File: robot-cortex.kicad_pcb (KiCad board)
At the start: 4 copper layers, 27.5 x 35.8 mm, 91 parts, among them IC1 THVD2410VDRCR, IC2 THVD2410VDRCR, IC3 THVD2410VDRCR, J1 USB4110GFA, M1 THRU_HOLE_PAD, M2 THRU_HOLE_PAD, Q1 SSM3K15F,LF, Q2 SS8050-G, U1 C2901617, U10 TPS63070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

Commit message: silk
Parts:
- moved R20 0.23 mm to (213.7, 121.3)
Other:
- board text added: "Vbat A B GND"
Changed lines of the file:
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@@
   )
   (footprint "robot-cortex:R_0402_1005Metric" (layer "F.Cu")
-    (at 213.7 121.5565)
+    (at 213.7 121.325)
     (descr "Resistor SMD 0402 (1005 Metric), square (rectangular) end terminal, IPC_7351 nominal, (Body size source: IPC-SM-782 page 72, https://www.pcb-3d.com/wordpress/wp-content/uploads/ipc-sm-782a_amendment_1_and_2.pdf), generated with kicad-footprint-generator")
     (tags "resistor")
@@
     )
   )
+  (gr_line (start 209.375 122.66875) (end 209.375 123.58125)
+    (stroke (width 0.15) (type default)) (layer "F.SilkS"))
+  (gr_line (start 197.75 122.66875) (end 197.75 123.58125)
+    (stroke (width 0.15) (type default)) (layer "F.SilkS"))
+  (gr_line (start 208.425 122.66875) (end 208.425 123.58125)
+    (stroke (width 0.15) (type default)) (layer "F.SilkS"))
+  (gr_line (start 200.6 122.66875) (end 200.6 123.58125)
+    (stroke (width 0.15) (type default)) (layer "F.SilkS"))
+  (gr_line (start 207.45 122.66875) (end 207.45 123.58125)
+    (stroke (width 0.15) (type default)) (layer "F.SilkS"))
+  (gr_line (start 210.3 122.66875) (end 210.3 123.58125)
+    (stroke (width 0.15) (type default)) (layer "F.SilkS"))
+  (gr_line (start 199.675 122.66875) (end 199.675 123.58125)
+    (stroke (width 0.15) (type default)) (layer "F.SilkS"))
+  (gr_line (start 198.725 122.66875) (end 198.725 123.58125)
+    (stroke (width 0.15) (type default)) (layer "F.SilkS"))
   (gr_line (start 191.91 89.7) (end 190.02 91.59)
     (stroke (width 0.1) (type default)) (layer "Edge.Cuts"))
@@
     (effects (font (size 0.762 0.762) (thickness 0.127)) (justify left bottom mirror))
   )
-  (gr_text "3V3" (at 195.75 101.69) (layer "B.SilkS")
+  (gr_text "3V3" (at 195.75 101.015) (layer "B.SilkS")
     (effects (font (size 0.635 0.635) (thickness 0.127)) (justify left bottom mirror))
   )
@@
     (effects (font (size 0.635 0.635) (thickness 0.127)) (justify left bottom mirror))
   )
-  (gr_text "IO0" (at 195.75 99.55) (layer "B.SilkS")
+  (gr_text "IO0" (at 195.75 98.875) (layer "B.SilkS")
     (effects (font (size 0.635 0.635) (thickness 0.127)) (justify left bottom mirror))
   )
@@
     (effects (font (size 0.635 0.635) (thickness 0.127)) (justify left bottom mirror))
   )
-  (gr_text "TDI" (at 195.75 96.6) (layer "B.SilkS")
+  (gr_text "TDI" (at 195.75 95.925) (layer "B.SilkS")
     (effects (font (size 0.635 0.635) (thickness 0.127)) (justify left bottom mirror))
   )
-  (gr_text "GND" (at 195.75 94.55) (layer "B.SilkS")
+  (gr_text "GND" (at 195.75 93.875) (layer "B.SilkS")
     (effects (font (size 0.635 0.635) (thickness 0.127)) (justify left bottom mirror))
   )
@@
     (effects (font (size 0.635 0.635) (thickness 0.127) bold) (justify left bottom mirror))
   )
-  (gr_text "TDO" (at 195.75 98.54) (layer "B.SilkS")
+  (gr_text "TDO" (at 195.75 97.865) (layer "B.SilkS")
     (effects (font (size 0.635 0.635) (thickness 0.127)) (justify left bottom mirror))
   )
@@
     (effects (font (size 0.635 0.635) (thickness 0.127)) (justify left bottom mirror))
   )
-  (gr_text "TMS" (at 195.75 97.57) (layer "B.SilkS")
+  (gr_text "TMS" (at 195.75 96.895) (layer "B.SilkS")
     (effects (font (size 0.635 0.635) (thickness 0.127)) (justify left bottom mirror))
   )
-  (gr_text "TCK" (at 195.75 95.65) (layer "B.SilkS")
+  (gr_text "TCK" (at 195.75 94.975) (layer "B.SilkS")
     (effects (font (size 0.635 0.635) (thickness 0.127)) (justify left bottom mirror))
   )
@@
     (effects (font (size 0.762 0.762) (thickness 0.127)) (justify left bottom mirror))
   )
-  (gr_text "EN" (at 195.75 100.57) (layer "B.SilkS")
+  (gr_text "EN" (at 195.75 99.895) (layer "B.SilkS")
     (effects (font (size 0.635 0.635) (thickness 0.127)) (justify left bottom mirror))
   )
+  (gr_text "Vbat\nA\nB\nGND" (at 200.925 122.50625 90) (layer "F.SilkS")
+    (effects (font (size 0.5842 0.5842) (thickness 0.0762)) (justify left bottom))
+  )
+  (gr_text "Vbat\nA\nB\nGND" (at 210.65 122.50625 90) (layer "F.SilkS")
+    (effects (font (size 0.5842 0.5842) (thickness 0.0762)) (justify left bottom))
+  )
   (gr_text "V3 R1" (at 210.43 91.72) (layer "F.SilkS")
     (effects (font (size 1 1) (thickness 0.2) bold) (justify left bottom))
@@
   (segment (start 203.727432 111.09) (end 204.405 111.09) (width 0.254) (layer "B.Cu") (net 61))
   (segment (start 194.4 116.75) (end 199.825 116.75) (width 0.254) (layer "B.Cu") (net 61))
-  (segment (start 213.45 120.3) (end 213.45 121.4315) (width 0.25) (layer "F.Cu") (net 62))
+  (segment (start 213.325 121.325) (end 213.325 122.4315) (width 0.25) (layer "F.Cu") (net 62))
+  (segment (start 213.45 121.2) (end 213.325 121.325) (width 0.25) (layer "F.Cu") (net 62))
   (segment (start 213.325 122.4315) (end 213.3 122.4565) (width 0.25) (layer "F.Cu") (net 62))
-  (segment (start 213.45 121.4315) (end 213.325 121.5565) (width 0.25) (layer "F.Cu") (net 62))
-  (segment (start 213.325 121.5565) (end 213.325 122.4315) (width 0.25) (layer "F.Cu") (net 62))
+  (segment (start 213.45 120.3) (end 213.45 121.2) (width 0.25) (layer "F.Cu") (net 62))
+  (segment (start 213.95 120.3) (end 213.95 121.2) (width 0.25) (layer "F.Cu") (net 63))
+  (segment (start 214.075 121.325) (end 214.075 122.4315) (width 0.25) (layer "F.Cu") (net 63))
   (segment (start 214.075 122.4315) (end 214.1 122.4565) (width 0.25) (layer "F.Cu") (net 63))
-  (segment (start 213.95 121.4315) (end 214.075 121.5565) (width 0.25) (layer "F.Cu") (net 63))
-  (segment (start 214.075 121.5565) (end 214.075 122.4315) (width 0.25) (layer "F.Cu") (net 63))
-  (segment (start 213.95 120.3) (end 213.95 121.4315) (width 0.25) (layer "F.Cu") (net 63))
+  (segment (start 213.95 121.2) (end 214.075 121.325) (width 0.25) (layer "F.Cu") (net 63))
   (segment (start 195.535 93.82) (end 195.535 92.98) (width 0.254) (layer "F.Cu") (net 93))
   (segment (start 196.105 92.97) (end 195.525 92.97) (width 0.254) (layer "F.Cu") (net 93))

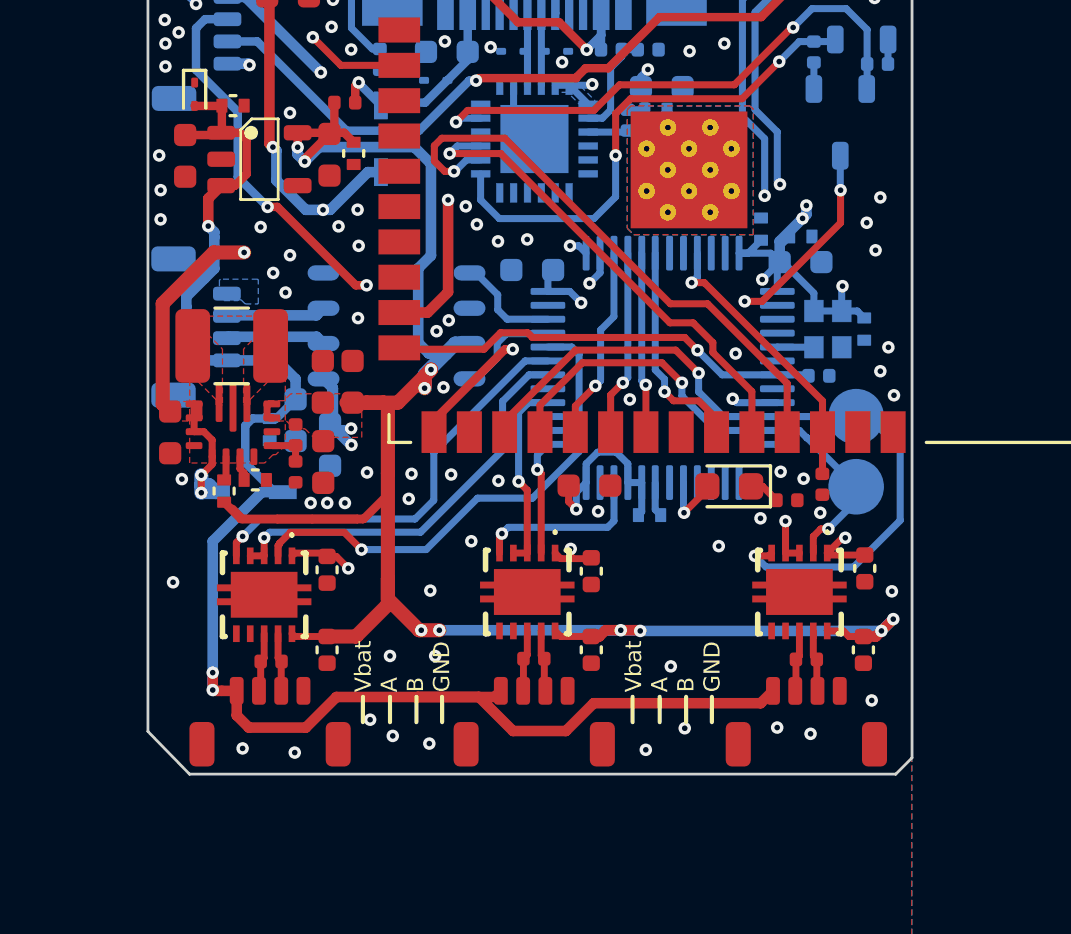
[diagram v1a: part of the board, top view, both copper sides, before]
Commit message: flipped connector layer
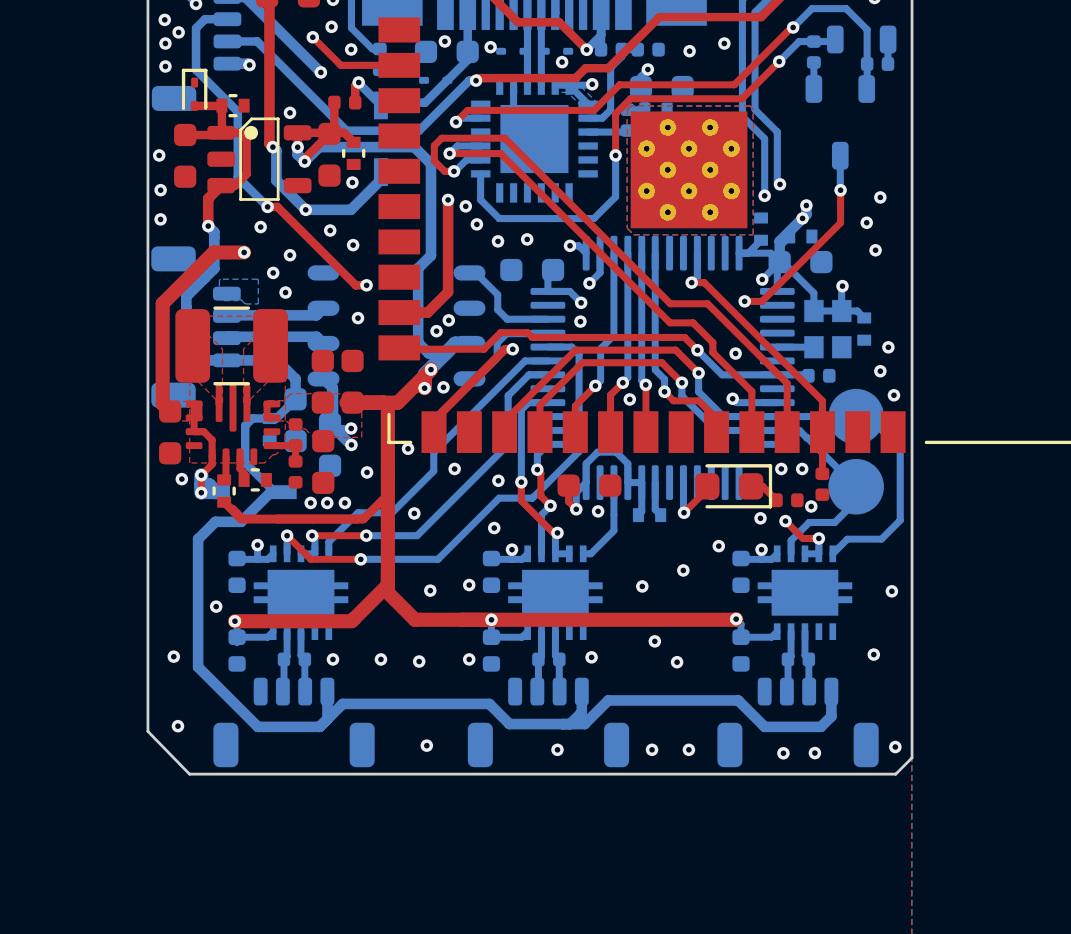
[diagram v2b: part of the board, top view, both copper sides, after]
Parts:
- C1, C28, C31, C36, C37, C38, IC1, IC2, IC3, R19, R20, R21, U12, U13, U14: moved to B.Cu
- moved C31 4.45 mm to (211.3, 118.2)
- moved C36 4.40 mm to (211.3, 121.0)
- moved C37 3.59 mm to (202.4, 118.2)
- moved C38 3.59 mm to (202.4, 121.0)
- moved C1 3.24 mm to (193.2, 118.2)
- moved C28 3.24 mm to (193.2, 121.0)
- moved IC1 1.33 mm to (195.5, 118.9)
- moved IC3 1.01 mm to (204.7, 118.9)
- moved U12 0.86 mm to (195.3, 122.5), turned to 180 degrees
- moved R19 0.84 mm to (195.3, 121.3), turned to 180 degrees
- moved R21 0.54 mm to (204.4, 121.3), turned to 180 degrees
- moved U14 0.51 mm to (204.4, 122.5), turned to 180 degrees
- moved U13 0.30 mm to (213.4, 122.5), turned to 180 degrees
- moved R20 0.29 mm to (213.4, 121.3), turned to 180 degrees
- moved IC2 0.20 mm to (213.6, 118.9)
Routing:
- net /UART1_TX: track 15.4 -> 11.4 mm, vias 1 -> 0
- net /UART2_TX: track 26.8 -> 23.0 mm, vias 2 -> 1
- net /+5V0: track 80.4 -> 76.9 mm, vias 10 -> 7
- net /UART3_TX: track 6.33 -> 3.18 mm, vias 1 -> 0
- net /VBAT: track 58.6 -> 60.7 mm, vias 3 -> 1
- net /UART1_DE: track 14.8 -> 13.1 mm, vias 1 -> 2
- net +3V3: track 56.4 -> 55.5 mm
- net /USART2_DE: track 8.50 -> 9.36 mm, vias 2 -> 3
- net /UART2_RX: track 18.3 -> 19.0 mm, vias 2 -> 1
- net /USART3_DE: track 6.88 -> 7.40 mm, vias 1 -> 2
- net /UART3_RX: track 4.12 -> 4.43 mm, vias 1 -> 2
- net /UART1_RX: track 17.9 -> 17.8 mm, vias 1 -> 2
- net GND: vias 88 -> 96

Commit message: bom cleanup - caps not hardcoded lcsc part, led replaced
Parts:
- C11, C13, C2, C34, C5, C7, C9: value C2998534 -> 10uF 0603
- C22, C24, C25, C27, C29, C30, C32, C33: value 10uF -> 10uF 0603
- D4, D7: value C84264 -> 150060GS84000
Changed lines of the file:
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@@
         (effects (font (size 1 1) (thickness 0.15)))
     )
-    (fp_text value "C84264" (at 0 1.43) (layer "F.Fab")
+    (fp_text value "150060GS84000" (at 0 1.43) (layer "F.Fab")
         (effects (font (size 1 1) (thickness 0.15)))
     )
@@
         (effects (font (size 1 1) (thickness 0.15)))
     )
-    (fp_text value "10uF " (at 0 1.43) (layer "F.Fab") hide
+    (fp_text value "10uF 0603 " (at 0 1.43) (layer "F.Fab") hide
         (effects (font (size 1 1) (thickness 0.15)))
     )
@@
         (effects (font (size 1 1) (thickness 0.15)))
     )
-    (fp_text value "10uF " (at 0 1.43 90) (layer "F.Fab") hide
+    (fp_text value "10uF 0603 " (at 0 1.43 90) (layer "F.Fab") hide
         (effects (font (size 1 1) (thickness 0.15)))
     )
@@
     (property "Sheetfile" "robot-cortex.kicad_sch")
     (property "Sheetname" "")
+    (property "Voltage" "10V")
     (property "ki_description" "Unpolarized capacitor")
     (property "ki_keywords" "cap capacitor")
@@
         (effects (font (size 1 1) (thickness 0.15)))
     )
-    (fp_text value "C2998534" (at 0 1.43 90) (layer "F.Fab") hide
+    (fp_text value "10uF 0603" (at 0 1.43 90) (layer "F.Fab") hide
         (effects (font (size 1 1) (thickness 0.15)))
     )
@@
         (effects (font (size 1 1) (thickness 0.15)))
     )
-    (fp_text value "10uF " (at 0 1.43 90) (layer "F.Fab") hide
+    (fp_text value "10uF 0603 " (at 0 1.43 90) (layer "F.Fab") hide
         (effects (font (size 1 1) (thickness 0.15)))
     )
@@
         (effects (font (size 1 1) (thickness 0.15)))
     )
-    (fp_text value "10uF " (at 0 1.43 90) (layer "F.Fab") hide
+    (fp_text value "10uF 0603 " (at 0 1.43 90) (layer "F.Fab") hide
         (effects (font (size 1 1) (thickness 0.15)))
     )
@@
         (effects (font (size 1 1) (thickness 0.15)))
     )
-    (fp_text value "10uF " (at 0 1.43) (layer "F.Fab") hide
+    (fp_text value "10uF 0603 " (at 0 1.43) (layer "F.Fab") hide
         (effects (font (size 1 1) (thickness 0.15)))
     )
@@
     (property "Sheetfile" "robot-cortex.kicad_sch")
     (property "Sheetname" "")
+    (property "Voltage" "10V")
     (property "ki_description" "Unpolarized capacitor")
     (property "ki_keywords" "cap capacitor")
@@
         (effects (font (size 1 1) (thickness 0.15)))
     )
-    (fp_text value "C2998534" (at 0 1.43) (layer "F.Fab") hide
+    (fp_text value "10uF 0603" (at 0 1.43) (layer "F.Fab") hide
         (effects (font (size 1 1) (thickness 0.15)))
     )
@@
     (property "Sheetfile" "robot-cortex.kicad_sch")
     (property "Sheetname" "")
+    (property "Voltage" "10V")
     (property "ki_description" "Unpolarized capacitor")
     (property "ki_keywords" "cap capacitor")
@@
         (effects (font (size 1 1) (thickness 0.15)))
     )
-    (fp_text value "C2998534" (at 0 1.43 90) (layer "F.Fab") hide
+    (fp_text value "10uF 0603" (at 0 1.43 90) (layer "F.Fab") hide
         (effects (font (size 1 1) (thickness 0.15)))
     )
@@
         (effects (font (size 1 1) (thickness 0.15)))
     )
-    (fp_text value "C84264" (at 0 1.43) (layer "F.Fab")
+    (fp_text value "150060GS84000" (at 0 1.43) (layer "F.Fab")
         (effects (font (size 1 1) (thickness 0.15)))
     )
@@
         (effects (font (size 1 1) (thickness 0.15)))
     )
-    (fp_text value "10uF " (at 0 1.43 90) (layer "F.Fab") hide
+    (fp_text value "10uF 0603 " (at 0 1.43 90) (layer "F.Fab") hide
         (effects (font (size 1 1) (thickness 0.15)))
     )
@@
         (effects (font (size 1 1) (thickness 0.15)))
     )
-    (fp_text value "10uF " (at 0 1.43) (layer "F.Fab") hide
+    (fp_text value "10uF 0603 " (at 0 1.43) (layer "F.Fab") hide
         (effects (font (size 1 1) (thickness 0.15)))
     )
@@
         (effects (font (size 1 1) (thickness 0.15)))
     )
-    (fp_text value "10uF " (at 0 1.43) (layer "F.Fab") hide
+    (fp_text value "10uF 0603 " (at 0 1.43) (layer "F.Fab") hide
         (effects (font (size 1 1) (thickness 0.15)))
     )
@@
     (property "Sheetfile" "robot-cortex.kicad_sch")
     (property "Sheetname" "")
+    (property "Voltage" "10V")
     (property "ki_description" "Unpolarized capacitor")
     (property "ki_keywords" "cap capacitor")
@@
         (effects (font (size 1 1) (thickness 0.15)) (justify mirror))
     )
-    (fp_text value "C2998534" (at 0 -1.43 90) (layer "B.Fab") hide
+    (fp_text value "10uF 0603" (at 0 -1.43 90) (layer "B.Fab") hide
         (effects (font (size 1 1) (thickness 0.15)) (justify mirror))
     )
@@
     (property "Sheetfile" "robot-cortex.kicad_sch")
     (property "Sheetname" "")
+    (property "Voltage" "10V")
     (property "ki_description" "Unpolarized capacitor")
     (property "ki_keywords" "cap capacitor")
@@
         (effects (font (size 1 1) (thickness 0.15)) (justify mirror))
     )
-    (fp_text value "C2998534" (at 0 -1.43) (layer "B.Fab") hide
+    (fp_text value "10uF 0603" (at 0 -1.43) (layer "B.Fab") hide
         (effects (font (size 1 1) (thickness 0.15)) (justify mirror))
     )
@@
     (property "Sheetfile" "robot-cortex.kicad_sch")
     (property "Sheetname" "")
+    (property "Voltage" "10V")
     (property "ki_description" "Unpolarized capacitor")
     (property "ki_keywords" "cap capacitor")
@@
         (effects (font (size 1 1) (thickness 0.15)) (justify mirror))
     )
-    (fp_text value "C2998534" (at 0 -1.43) (layer "B.Fab") hide
+    (fp_text value "10uF 0603" (at 0 -1.43) (layer "B.Fab") hide
         (effects (font (size 1 1) (thickness 0.15)) (justify mirror))
     )
@@
     (property "Sheetfile" "robot-cortex.kicad_sch")
     (property "Sheetname" "")
+    (property "Voltage" "10V")
     (property "ki_description" "Unpolarized capacitor")
     (property "ki_keywords" "cap capacitor")
@@
         (effects (font (size 1 1) (thickness 0.15)) (justify mirror))
     )
-    (fp_text value "C2998534" (at 0 -1.43 90) (layer "B.Fab") hide
+    (fp_text value "10uF 0603" (at 0 -1.43 90) (layer "B.Fab") hide
         (effects (font (size 1 1) (thickness 0.15)) (justify mirror))
     )

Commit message: more bom
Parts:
- Q2: value SS8050-G -> SSM3K15F,LF
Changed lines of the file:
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@@
         (effects (font (size 1 1) (thickness 0.15)) (justify mirror))
     )
-    (fp_text value "SS8050-G" (at 0 -2.4 90) (layer "B.Fab") hide
+    (fp_text value "SSM3K15F,LF" (at 0 -2.4 90) (layer "B.Fab") hide
         (effects (font (size 1 1) (thickness 0.15)) (justify mirror))
     )

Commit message: final bom cleanup
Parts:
- L1, L2: value 1277AS-H-1R0M=P2 -> 1uH
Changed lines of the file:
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@@
     (descr "Inductor SMD 1210 (3225 Metric), square (rectangular) end terminal, IPC_7351 nominal, (Body size source: http://www.tortai-tech.com/upload/download/2011102023233369053.pdf), generated with kicad-footprint-generator")
     (tags "inductor")
-    (property "MPN" "ETQ-P3M3R3KVP")
+    (property "DCR" "45mOhm")
+    (property "MPN" "1277AS-H-1R0M=P2")
     (property "Sheetfile" "PSU_TPS63070RNMR.kicad_sch")
     (property "Sheetname" "PSU_TPS63070RNMR")
@@
         (effects (font (size 1 1) (thickness 0.15)))
     )
-    (fp_text value "1277AS-H-1R0M=P2" (at 0.14 -0.655 90) (layer "F.Fab")
+    (fp_text value "1uH" (at 0.14 -0.655 90) (layer "F.Fab")
         (effects (font (size 0.2 0.2) (thickness 0.05)))
     )
@@
     (descr "Inductor SMD 1210 (3225 Metric), square (rectangular) end terminal, IPC_7351 nominal, (Body size source: http://www.tortai-tech.com/upload/download/2011102023233369053.pdf), generated with kicad-footprint-generator")
     (tags "inductor")
-    (property "MPN" "ETQ-P3M3R3KVP")
+    (property "DCR" "45mOhm")
+    (property "MPN" "1277AS-H-1R0M=P2")
     (property "Sheetfile" "PSU_TPS63070RNMR.kicad_sch")
     (property "Sheetname" "PSU_TPS63070RNMR1")
@@
         (effects (font (size 1 1) (thickness 0.15)))
     )
-    (fp_text value "1277AS-H-1R0M=P2" (at 0.14 -0.655) (layer "F.Fab")
+    (fp_text value "1uH" (at 0.14 -0.655) (layer "F.Fab")
         (effects (font (size 0.2 0.2) (thickness 0.05)))
     )

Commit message: found better part
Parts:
- IC1, IC2, IC3: value THVD2410VDRCR -> THVD2450VDRCR
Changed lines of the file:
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@@
     (property "Height" "1")
     (property "Manufacturer_Name" "Texas Instruments")
-    (property "Manufacturer_Part_Number" "THVD2410VDRCR")
+    (property "Manufacturer_Part_Number" "THVD2450VDRCR")
     (property "Mouser Part Number" "595-THVD2410VDRCR")
     (property "Mouser Price/Stock" "https://www.mouser.co.uk/ProductDetail/Texas-Instruments/THVD2410VDRCR?qs=Jm2GQyTW%2FbhjNqkbRGOzgg%3D%3D")
@@
         (effects (font (size 1.27 1.27) (thickness 0.15)) (justify mirror))
     )
-    (fp_text value "THVD2410VDRCR" (at 0 -2.54 90) (layer "B.SilkS") hide
+    (fp_text value "THVD2450VDRCR" (at 0 -2.54 90) (layer "B.SilkS") hide
         (effects (font (size 1.27 1.27) (thickness 0.15)) (justify mirror))
     )
@@
     (property "Height" "1")
     (property "Manufacturer_Name" "Texas Instruments")
-    (property "Manufacturer_Part_Number" "THVD2410VDRCR")
+    (property "Manufacturer_Part_Number" "THVD2450VDRCR")
     (property "Mouser Part Number" "595-THVD2410VDRCR")
     (property "Mouser Price/Stock" "https://www.mouser.co.uk/ProductDetail/Texas-Instruments/THVD2410VDRCR?qs=Jm2GQyTW%2FbhjNqkbRGOzgg%3D%3D")
@@
         (effects (font (size 1.27 1.27) (thickness 0.15)) (justify mirror))
     )
-    (fp_text value "THVD2410VDRCR" (at 0 -2.54 90) (layer "B.SilkS") hide
+    (fp_text value "THVD2450VDRCR" (at 0 -2.54 90) (layer "B.SilkS") hide
         (effects (font (size 1.27 1.27) (thickness 0.15)) (justify mirror))
     )
@@
     (property "Height" "1")
     (property "Manufacturer_Name" "Texas Instruments")
-    (property "Manufacturer_Part_Number" "THVD2410VDRCR")
+    (property "Manufacturer_Part_Number" "THVD2450VDRCR")
     (property "Mouser Part Number" "595-THVD2410VDRCR")
     (property "Mouser Price/Stock" "https://www.mouser.co.uk/ProductDetail/Texas-Instruments/THVD2410VDRCR?qs=Jm2GQyTW%2FbhjNqkbRGOzgg%3D%3D")
@@
         (effects (font (size 1.27 1.27) (thickness 0.15)) (justify mirror))
     )
-    (fp_text value "THVD2410VDRCR" (at 0 -2.54 90) (layer "B.SilkS") hide
+    (fp_text value "THVD2450VDRCR" (at 0 -2.54 90) (layer "B.SilkS") hide
         (effects (font (size 1.27 1.27) (thickness 0.15)) (justify mirror))
     )

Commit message: curvy
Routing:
- net /+5V0: track 76.9 -> 70.4 mm
- net +3V3: track 55.5 -> 53.9 mm
- net /ESP32/IO0: track 40.1 -> 39.3 mm
- net /ESP32/EN: track 30.5 -> 29.8 mm
- net /VDD_MIXED: track 29.8 -> 29.3 mm
